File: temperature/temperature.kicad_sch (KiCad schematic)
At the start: 4 parts

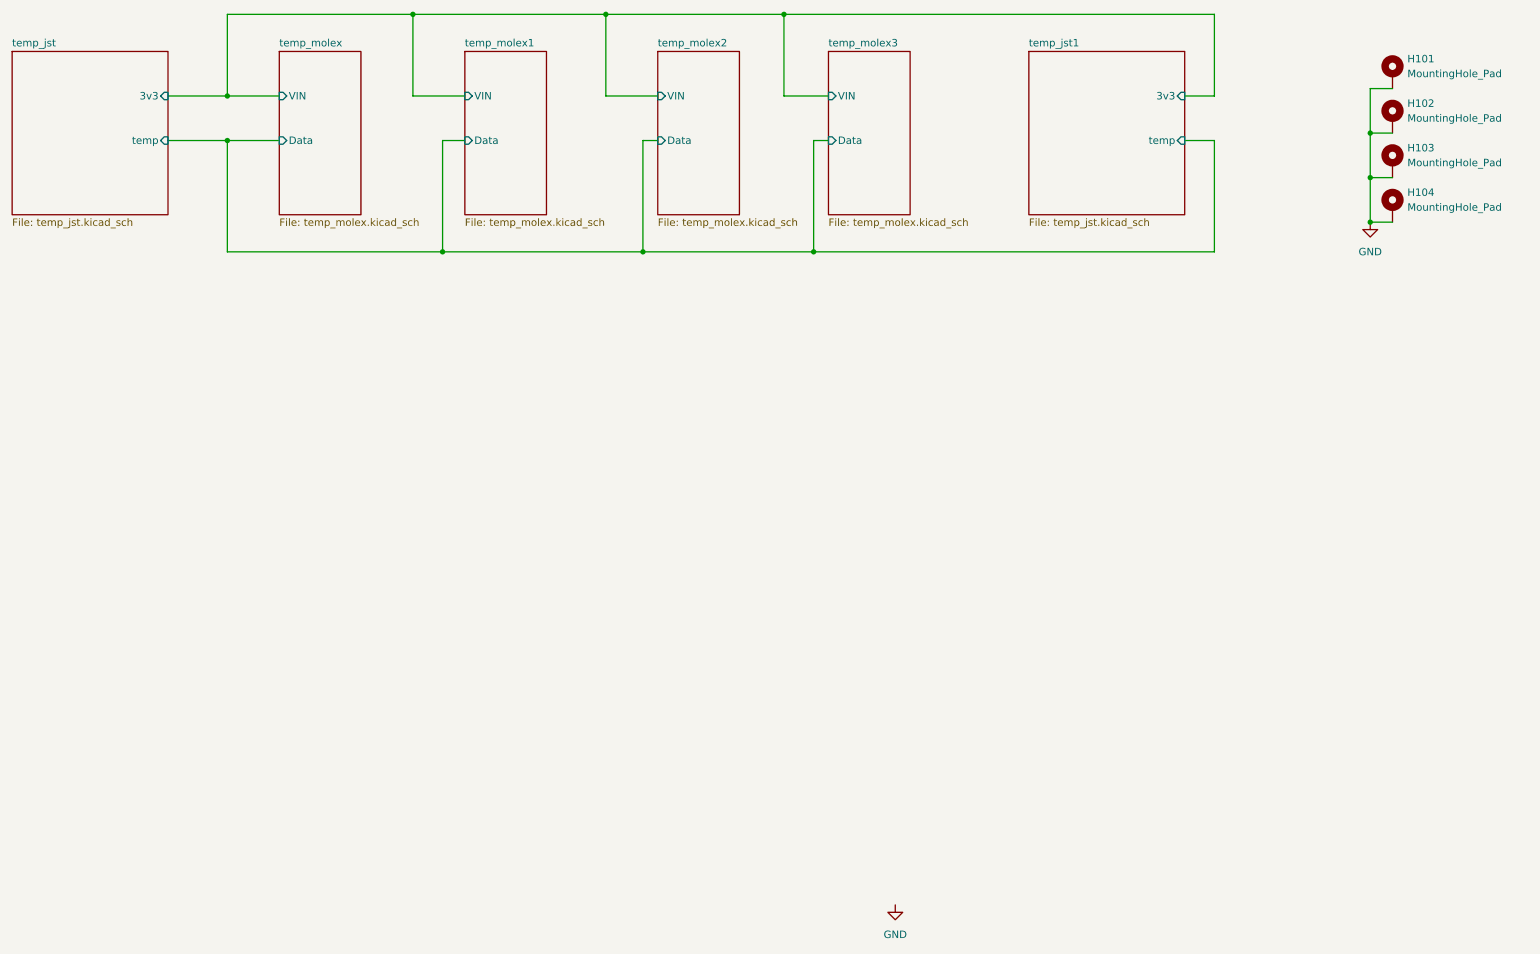
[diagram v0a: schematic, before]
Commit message: add old system temp connectors
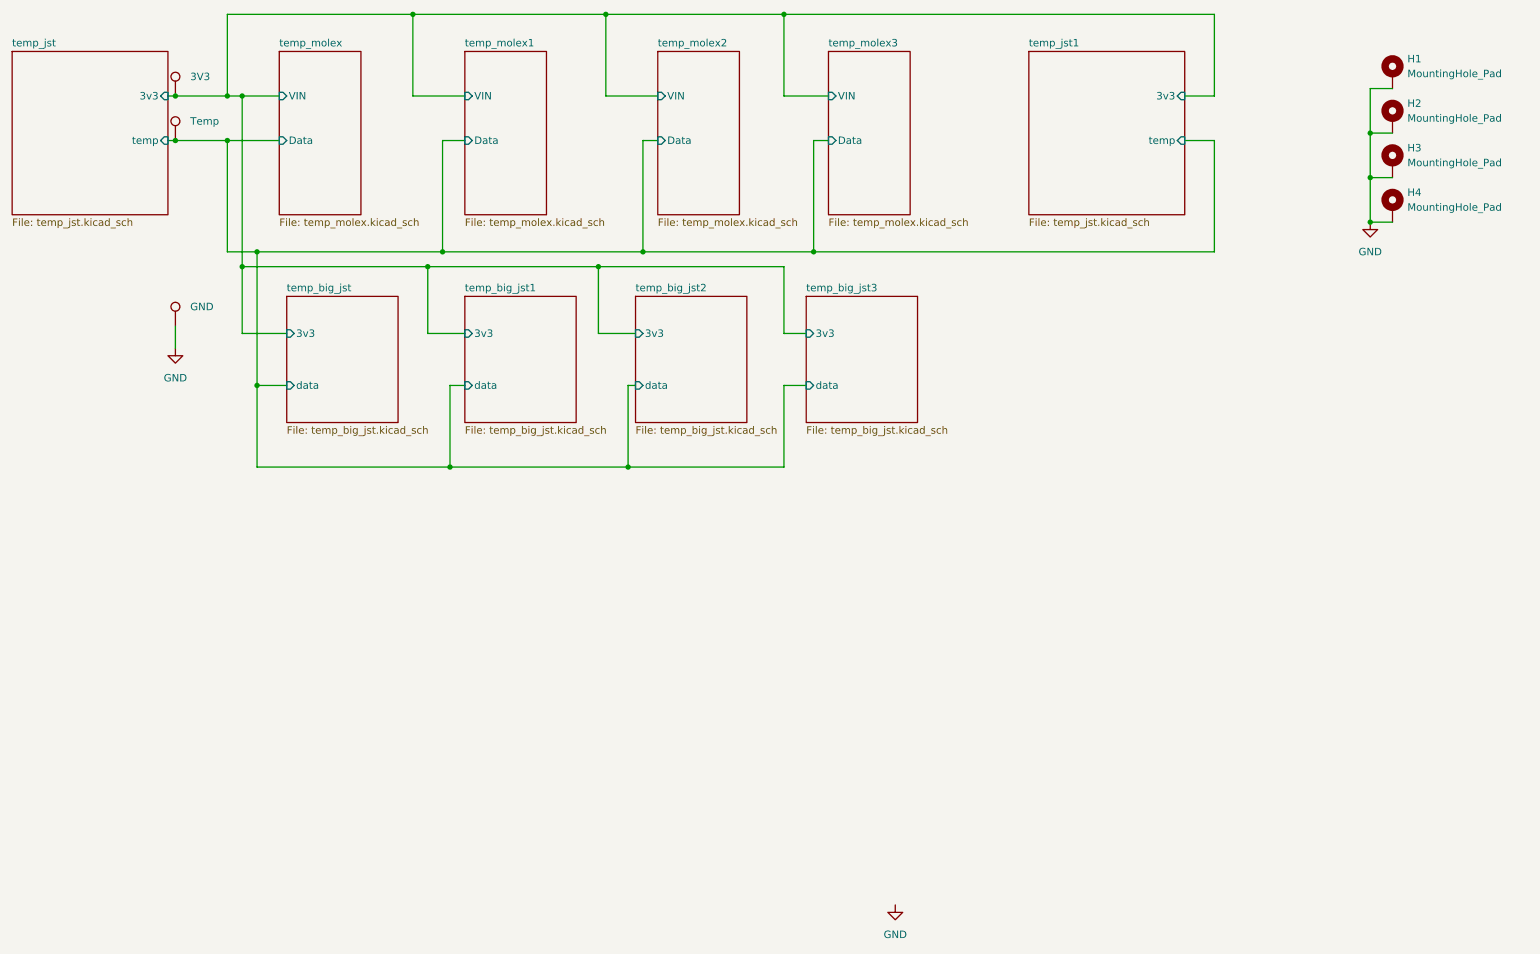
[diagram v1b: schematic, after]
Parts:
- added TP1, TP2, TP3: LabeledTestPoint, easyeda2kicad:LabeledTestPoint, symbol easyeda2kicad:LabeledTestPoint
- renumbered H101 to H1, H102 to H2, H103 to H3, H104 to H4
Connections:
- net GND: now also TP3.1
- new net temp_big_jst/3v3: TP1.1
- new net temp_big_jst/data: TP2.1
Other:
- added sheet temp_big_jst (temp_big_jst.kicad_sch)
- added sheet temp_big_jst1 (temp_big_jst.kicad_sch)
- added sheet temp_big_jst2 (temp_big_jst.kicad_sch)
- added sheet temp_big_jst3 (temp_big_jst.kicad_sch)
